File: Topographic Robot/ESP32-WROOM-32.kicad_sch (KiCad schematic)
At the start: 3 parts, among them U5 ESP32-WROOM-32

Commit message: Movement + Sensors
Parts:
- added U10: QMC5883L, symbol Sensors:QMC5883L
- added U11: MicroSD Card Reader, symbol Sensors:MicroSD_Card_Reader
- added U12: CCS811, symbol Sensors:CCS811
- added U13: MQ135, symbol Sensors:MQ135
- added U14: GY-NEO6MV2, symbol Sensors:GY-NEO6MV2
- added U7: DHT22, symbol Sensors:DHT22
- added U8: BH1750, symbol Sensors:BH1750
- added U9: MPU6050, symbol Sensors:MPU6050
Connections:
- net 3V3: now also U10. (VCC), U11. (SCLK), U12. (WAKE), U13. (VCC), U14. (VCC), U7. (VCC), U8. (VCC), U9. (XDA)
- net D21: now also U10. (VCC), U12. (WAKE), U8. (VCC), U9. (XDA)
- net D22: now also U10. (VCC), U12. (WAKE), U8. (VCC), U9. (XDA)
- net D26: now also U9. (XDA)
- net GND: now also U10. (VCC), U11. (SCLK), U12. (WAKE), U13. (VCC), U14. (VCC), U7. (VCC), U8. (VCC), U9. (XDA)
- new net D14: U11. (SCLK), U5. (VIN_5V)
- new net D16: U14. (VCC), U5. (VIN_5V)
- new net D17: U14. (VCC), U5. (VIN_5V)
- new net D18: U10. (VCC), U5. (VIN_5V)
- new net D19: U11. (SCLK), U5. (VIN_5V)
- new net D23: U11. (SCLK), U5. (VIN_5V)
- new net D25: U12. (WAKE), U5. (VIN_5V)
- new net D32: U12. (WAKE), U5. (VIN_5V)
- new net D33: U12. (WAKE), U5. (VIN_5V)
- new net D34: U13. (VCC), U5. (VIN_5V)
- new net D35: U13. (VCC), U5. (VIN_5V)
- new net D4: U5. (VIN_5V), U7. (VCC)
- new net D5: U11. (SCLK), U5. (VIN_5V)
- no-connect marks 24 -> 15
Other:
- note added: "BH1750"
- note added: "CCS811"
- note added: "DHT22"
- note added: "GY-NEO6MV2"
- note added: "MPU6050"
- note added: "MQ135"
- note added: "MicroSD"
- note added: "QMC5883L"

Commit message: THEY ARE QUAD TRISTATE BUFFERS TOOO SOOOOO I GOT 400 TRISTATE BUFFERS!!!!!
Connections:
- new net D13: U5. (VIN_5V)
- new net D15: U5. (VIN_5V)
- no-connect marks 15 -> 14
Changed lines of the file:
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@@
-	)
-	(no_connect
-		(at 44.45 38.1)
 	)
 	(no_connect
@@
 		)
 	)
-	(global_label "D14"
+	(global_label "D15"
 		(shape output)
 		(at 44.45 43.18 0)
@@
 			(effects
 				(font
+					(size 1.27 1.27)
+				)
+				(justify left)
+				(hide yes)
+			)
+		)
+	)
+	(global_label "D13"
+		(shape output)
+		(at 44.45 38.1 0)
+		(fields_autoplaced yes)
+		(effects
+			(font
+				(size 1.27 1.27)
+			)
+			(justify left)
+		)
+		(property "Intersheetrefs" "${INTERSHEET_REFS}"
+			(at 51.1242 38.1 0)
+			(effects
+				(font

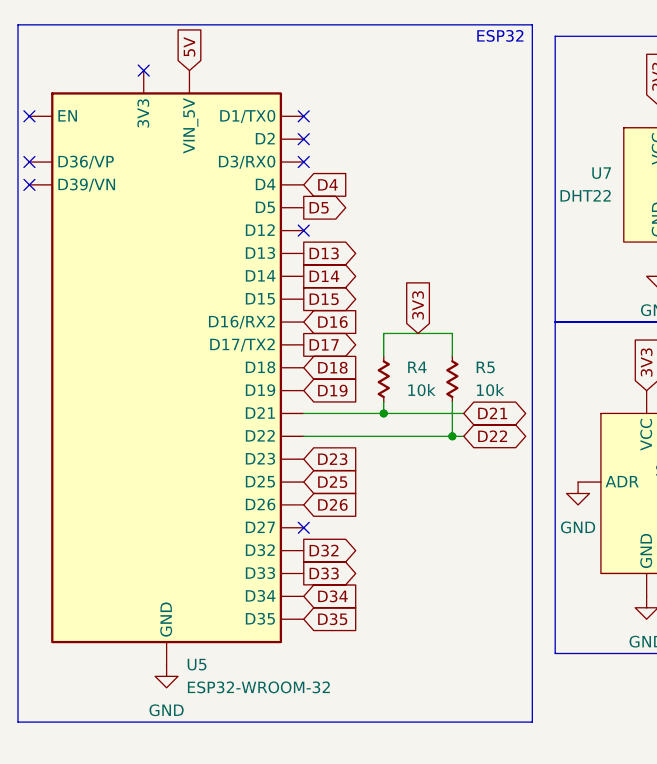
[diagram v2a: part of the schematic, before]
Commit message: Parallel > USB ?!
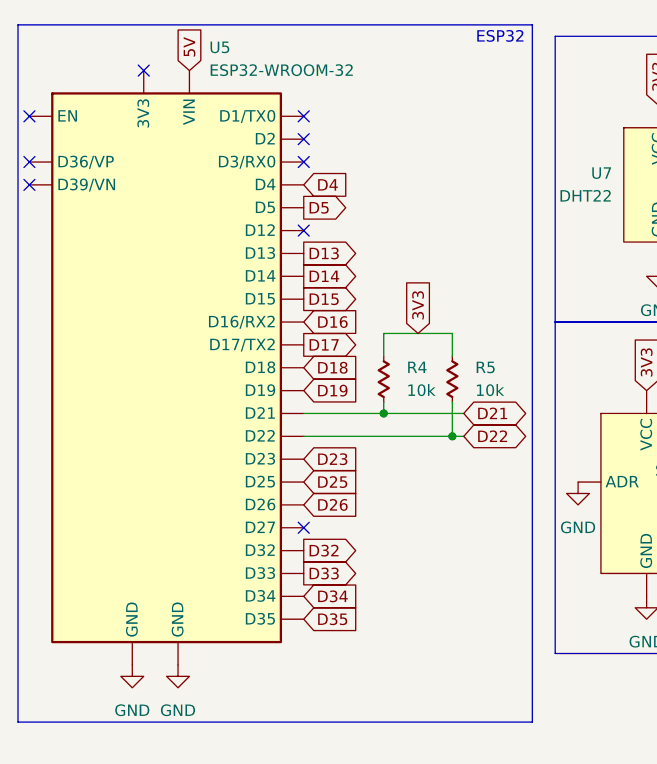
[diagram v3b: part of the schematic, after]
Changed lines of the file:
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@@
 		(fields_autoplaced yes)
 		(property "Reference" "U5"
-			(at 31.4041 83.82 0)
+			(at 33.9441 15.24 0)
 			(effects
 				(font
@@
 		)
 		(property "Value" "ESP32-WROOM-32"
-			(at 31.4041 86.36 0)
+			(at 33.9441 17.78 0)
 			(effects
 				(font
@@
 		(pin ""
 		)
-		(instances
-			(project "Topographic Robot"
+		(pin ""
+		)
+		(instances
+			(project ""
 				(path "/67e33313-0ce8-4ff5-8d50-46dc6ab8d472/b10fdbae-69f4-4df8-8c58-54772b8ff5c0"
 					(reference "U5")
@@
 	(symbol
 		(lib_id "power:GND")
-		(at 29.21 83.82 0)
+		(at 30.48 83.82 0)
 		(unit 1)
 		(exclude_from_sim no)
@@
 		(fields_autoplaced yes)
 		(property "Reference" "#PWR05"
-			(at 29.21 90.17 0)
+			(at 30.48 90.17 0)
 			(effects
 				(font
@@
 		)
 		(property "Value" "GND"
-			(at 29.21 88.9 0)
-			(effects
-				(font
-					(size 1.27 1.27)
-				)
-			)
-		)
-		(property "Footprint" ""
-			(at 29.21 83.82 0)
-			(effects
-				(font
-					(size 1.27 1.27)
-				)
-				(hide yes)
-			)
-		)
-		(property "Datasheet" ""
-			(at 29.21 83.82 0)
+			(at 30.48 88.9 0)
+			(effects
+				(font
+					(size 1.27 1.27)
+				)
+			)
+		)
+		(property "Footprint" ""
+			(at 30.48 83.82 0)
+			(effects
+				(font
+					(size 1.27 1.27)
+				)
+				(hide yes)
+			)
+		)
+		(property "Datasheet" ""
+			(at 30.48 83.82 0)
 			(effects
 				(font
@@
 		)
 		(property "Description" "Power symbol creates a global label with name \"GND\" , ground"
-			(at 29.21 83.82 0)
+			(at 30.48 83.82 0)
 			(effects
 				(font
@@
 					(unit 1)
 				)
+			)
+		)
+	)
+	(symbol
+		(lib_id "power:GND")
+		(at 25.4 83.82 0)
+		(unit 1)
+		(exclude_from_sim no)
+		(in_bom yes)
+		(on_board yes)
+		(dnp no)
+		(fields_autoplaced yes)
+		(property "Reference" "#PWR038"
+			(at 25.4 90.17 0)
+			(effects
+				(font
+					(size 1.27 1.27)
+				)
+				(hide yes)
+			)
+		)
+		(property "Value" "GND"
+			(at 25.4 88.9 0)
+			(effects
+				(font
+					(size 1.27 1.27)
+				)
+			)
+		)
+		(property "Footprint" ""
+			(at 25.4 83.82 0)
+			(effects
+				(font
+					(size 1.27 1.27)
+				)
+				(hide yes)
+			)
+		)
+		(property "Datasheet" ""
+			(at 25.4 83.82 0)
+			(effects
+				(font
+					(size 1.27 1.27)
+				)
+				(hide yes)
+			)
+		)
+		(property "Description" "Power symbol creates a global label with name \"GND\" , ground"
+			(at 25.4 83.82 0)
+			(effects
+				(font
+					(size 1.27 1.27)
+				)
+				(hide yes)
+			)
+		)
+		(pin "1"
+		)
+		(instances
+			(project "Topographic Robot"
+				(path "/67e33313-0ce8-4ff5-8d50-46dc6ab8d472/b10fdbae-69f4-4df8-8c58-54772b8ff5c0"
+					(reference "#PWR038")
+					(unit 1)
+				)
